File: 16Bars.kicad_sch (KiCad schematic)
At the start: 47 parts, among them IC1 CD4033BE, IC2 CD4033BE, IC3 CD4510BE, IC4 CD4510BE, IC5 CD4510BE, J1 3.5mm_Mono_Switched, J2 Conn_02x05_Odd_Even, Q1 2N3904, Q2 2N3904, Q3 2N3904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

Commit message: Fabrication Output for Rev 2.0
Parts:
- C1: footprint Capacitor_THT:C_Radial_D5.0mm_H11.0mm_P2.00mm -> Capacitor_THT:CP_Radial_D5.0mm_P2.00mm
- C11: Manufacturer_Part_Number (none) -> C13533
- C2, C3, C4, C5, C6: Manufacturer_Part_Number (none) -> C1525
- D1, D3, D4, D5: Manufacturer_Part_Number (none) -> C191023
- D2: Manufacturer_Part_Number (none) -> C2290
- Q1, Q2, Q3: Manufacturer_Part_Number (none) -> C9634
- R1, R11, R13, R14, R16, R17, R18, R19, R2, R20, R3, R4, R6: Manufacturer_Part_Number (none) -> C25744
- R10, R7, R8, R9: LCSC (none) -> C25744; Manufacturer_Part_Number (none) -> C25744
- R12, R15: Manufacturer_Part_Number (none) -> C4109
- R5: Manufacturer_Part_Number (none) -> C25792
- SW2: value SW_SPDT - EG1249 -> SW_SPDT-EG1249
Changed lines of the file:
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@@
+      (effects (font (size 1.27 1.27)) hide)
+    )
+    (property "Manufacturer_Part_Number" "C9634" (id 5) (at 228.6 133.35 0)
       (effects (font (size 1.27 1.27)) hide)
     )
@@
       (effects (font (size 1.27 1.27)) hide)
     )
+    (property "LCSC" "C25744" (id 4) (at 54.61 134.62 0)
+      (effects (font (size 1.27 1.27)) hide)
+    )
+    (property "Manufacturer_Part_Number" "C25744" (id 5) (at 54.61 134.62 0)
+      (effects (font (size 1.27 1.27)) hide)
+    )
     (pin "1")
     (pin "2")
@@
     )
     (property "LCSC" "C25744" (id 4) (at 127 128.27 90)
+      (effects (font (size 1.27 1.27)) hide)
+    )
+    (property "Manufacturer_Part_Number" "C25744" (id 5) (at 127 128.27 0)
       (effects (font (size 1.27 1.27)) hide)
     )
@@
       (effects (font (size 1.27 1.27)) hide)
     )
+    (property "Manufacturer_Part_Number" "C25744" (id 5) (at 194.31 29.21 0)
+      (effects (font (size 1.27 1.27)) hide)
+    )
     (pin "1")
     (pin "2")
@@
       (effects (font (size 1.27 1.27)) hide)
     )
+    (property "Manufacturer_Part_Number" "C25744" (id 5) (at 132.08 33.02 0)
+      (effects (font (size 1.27 1.27)) hide)
+    )
     (pin "1")
     (pin "2")
@@
       (effects (font (size 1.27 1.27)) hide)
     )
+    (property "Manufacturer_Part_Number" "C191023" (id 5) (at 45.72 26.67 0)
+      (effects (font (size 1.27 1.27)) hide)
+    )
     (pin "1")
     (pin "2")
@@
     )
     (property "LCSC" "C25744" (id 4) (at 135.89 119.38 90)
+      (effects (font (size 1.27 1.27)) hide)
+    )
+    (property "Manufacturer_Part_Number" "C25744" (id 5) (at 135.89 119.38 0)
       (effects (font (size 1.27 1.27)) hide)
     )
@@
       (effects (font (size 1.27 1.27)) (justify left))
     )
-    (property "Value" "SW_SPDT - EG1249" (id 1) (at 82.55 69.8499 0)
+    (property "Value" "SW_SPDT-EG1249" (id 1) (at 82.55 69.8499 0)
       (effects (font (size 1.27 1.27)) (justify left))
     )
@@
       (effects (font (size 1.27 1.27)) (justify left))
     )
-    (property "Footprint" "Capacitor_THT:C_Radial_D5.0mm_H11.0mm_P2.00mm" (id 2) (at 41.91 180.34 0)
+    (property "Footprint" "Capacitor_THT:CP_Radial_D5.0mm_P2.00mm" (id 2) (at 41.91 180.34 0)
       (effects (font (size 1.27 1.27)) hide)
     )
@@
     )
     (property "Datasheet" "~" (id 3) (at 24.13 134.62 0)
+      (effects (font (size 1.27 1.27)) hide)
+    )
+    (property "LCSC" "C25744" (id 4) (at 24.13 134.62 0)
+      (effects (font (size 1.27 1.27)) hide)
+    )
+    (property "Manufacturer_Part_Number" "C25744" (id 5) (at 24.13 134.62 0)
       (effects (font (size 1.27 1.27)) hide)
     )
@@
       (effects (font (size 1.27 1.27)) hide)
     )
+    (property "Manufacturer_Part_Number" "C191023" (id 5) (at 120.65 102.87 0)
+      (effects (font (size 1.27 1.27)) hide)
+    )
     (pin "1")
     (pin "2")
@@
     )
     (property "LCSC" "C9634" (id 4) (at 133.35 132.08 0)
+      (effects (font (size 1.27 1.27)) hide)
+    )
+    (property "Manufacturer_Part_Number" "C9634" (id 5) (at 133.35 132.08 0)
       (effects (font (size 1.27 1.27)) hide)
     )
@@
       (effects (font (size 1.27 1.27)) hide)
     )
+    (property "Manufacturer_Part_Number" "C1525" (id 5) (at 177.8 62.23 0)
+      (effects (font (size 1.27 1.27)) hide)
+    )
     (pin "1")
     (pin "2")
@@
       (effects (font (size 1.27 1.27)) hide)
     )
+    (property "Manufacturer_Part_Number" "C1525" (id 5) (at 181.61 24.13 0)
+      (effects (font (size 1.27 1.27)) hide)
+    )
     (pin "1")
     (pin "2")
@@
       (effects (font (size 1.27 1.27)) hide)
     )
+    (property "Manufacturer_Part_Number" "C25744" (id 5) (at 219.71 133.35 0)
+      (effects (font (size 1.27 1.27)) hide)
+    )
     (pin "1")
     (pin "2")
@@
     )
     (property "LCSC" "C25744" (id 4) (at 238.76 128.27 90)
+      (effects (font (size 1.27 1.27)) hide)
+    )
+    (property "Manufacturer_Part_Number" "C25744" (id 5) (at 238.76 128.27 0)
       (effects (font (size 1.27 1.27)) hide)
     )
@@
       (effects (font (size 1.27 1.27)) hide)
     )
+    (property "Manufacturer_Part_Number" "C25744" (id 5) (at 26.67 35.56 0)
+      (effects (font (size 1.27 1.27)) hide)
+    )
     (pin "1")
     (pin "2")
@@
     )
     (property "LCSC" "C1525" (id 4) (at 76.2 130.81 90)
+      (effects (font (size 1.27 1.27)) hide)
+    )
+    (property "Manufacturer_Part_Number" "C1525" (id 5) (at 76.2 130.81 0)
       (effects (font (size 1.27 1.27)) hide)
     )
@@
       (effects (font (size 1.27 1.27)) hide)
     )
+    (property "Manufacturer_Part_Number" "C25744" (id 5) (at 231.14 124.46 0)
+      (effects (font (size 1.27 1.27)) hide)
+    )
     (pin "1")
     (pin "2")
@@
     )
     (property "LCSC" "C25744" (id 4) (at 250.19 119.38 90)
+      (effects (font (size 1.27 1.27)) hide)
+    )
+    (property "Manufacturer_Part_Number" "C25744" (id 5) (at 250.19 119.38 0)
       (effects (font (size 1.27 1.27)) hide)
     )
@@
       (effects (font (size 1.27 1.27)) hide)
     )
+    (property "Manufacturer_Part_Number" "C25744" (id 5) (at 35.56 31.75 0)
+      (effects (font (size 1.27 1.27)) hide)
+    )
     (pin "1")
     (pin "2")
@@
       (effects (font (size 1.27 1.27)) hide)
     )
+    (property "LCSC" "C25744" (id 4) (at 26.67 134.62 0)
+      (effects (font (size 1.27 1.27)) hide)
+    )
+    (property "Manufacturer_Part_Number" "C25744" (id 5) (at 26.67 134.62 0)
+      (effects (font (size 1.27 1.27)) hide)
+    )
     (pin "1")
     (pin "2")
@@
     )
     (property "LCSC" "C4109" (id 4) (at 93.98 134.62 90)
+      (effects (font (size 1.27 1.27)) hide)
+    )
+    (property "Manufacturer_Part_Number" "C4109" (id 5) (at 93.98 134.62 0)
       (effects (font (size 1.27 1.27)) hide)
     )
@@
     )
     (property "LCSC" "C25744" (id 4) (at 85.09 53.34 90)
+      (effects (font (size 1.27 1.27)) hide)
+    )
+    (property "Manufacturer_Part_Number" "C25744" (id 5) (at 85.09 53.34 0)
       (effects (font (size 1.27 1.27)) hide)
     )
@@
       (effects (font (size 1.27 1.27)) hide)
     )
+    (property "Manufacturer_Part_Number" "C25792" (id 5) (at 198.12 133.35 0)
+      (effects (font (size 1.27 1.27)) hide)
+    )
     (pin "1")
     (pin "2")
@@
     )
     (property "Datasheet" "~" (id 3) (at 57.15 134.62 0)
+      (effects (font (size 1.27 1.27)) hide)
+    )
+    (property "LCSC" "C25744" (id 4) (at 57.15 134.62 0)
+      (effects (font (size 1.27 1.27)) hide)
+    )
+    (property "Manufacturer_Part_Number" "C25744" (id 5) (at 57.15 134.62 0)
       (effects (font (size 1.27 1.27)) hide)
     )
@@
     )
     (property "LCSC" "C9634" (id 4) (at 247.65 128.27 0)
+      (effects (font (size 1.27 1.27)) hide)
+    )
+    (property "Manufacturer_Part_Number" "C9634" (id 5) (at 247.65 128.27 0)
       (effects (font (size 1.27 1.27)) hide)
     )
@@
       (effects (font (size 1.27 1.27)) hide)
     )
+    (property "Manufacturer_Part_Number" "C2290" (id 5) (at 38.1 199.39 0)
+      (effects (font (size 1.27 1.27)) hide)
+    )
     (pin "1")
     (pin "2")
@@
     )
     (property "LCSC" "C191023" (id 4) (at 205.74 133.35 0)
+      (effects (font (size 1.27 1.27)) hide)
+    )
+    (property "Manufacturer_Part_Number" "C191023" (id 5) (at 205.74 133.35 0)
       (effects (font (size 1.27 1.27)) hide)
     )
@@
       (effects (font (size 1.27 1.27)) hide)
     )
+    (property "Manufacturer_Part_Number" "C25744" (id 5) (at 193.04 73.66 0)
+      (effects (font (size 1.27 1.27)) hide)
+    )
     (pin "1")
     (pin "2")
@@
     )
     (property "LCSC" "C4109" (id 4) (at 49.53 199.39 90)
+      (effects (font (size 1.27 1.27)) hide)
+    )
+    (property "Manufacturer_Part_Number" "C4109" (id 5) (at 49.53 199.39 0)
       (effects (font (size 1.27 1.27)) hide)
     )
@@
     )
     (property "LCSC" "C1525" (id 4) (at 45.72 135.89 90)
+      (effects (font (size 1.27 1.27)) hide)
+    )
+    (property "Manufacturer_Part_Number" "C1525" (id 5) (at 45.72 135.89 0)
       (effects (font (size 1.27 1.27)) hide)
     )
@@
       (effects (font (size 1.27 1.27)) hide)
     )
+    (property "Manufacturer_Part_Number" "C191023" (id 5) (at 38.1 26.67 0)
+      (effects (font (size 1.27 1.27)) hide)
+    )
     (pin "1")
     (pin "2")
@@
       (effects (font (size 1.27 1.27)) hide)
     )
+    (property "Manufacturer_Part_Number" "C1525" (id 5) (at 34.29 54.61 0)
+      (effects (font (size 1.27 1.27)) hide)
+    )
     (pin "1")
     (pin "2")
@@
       (effects (font (size 1.27 1.27)) hide)
     )
+    (property "Manufacturer_Part_Number" "C25744" (id 5) (at 129.54 73.66 0)
+      (effects (font (size 1.27 1.27)) hide)
+    )
     (pin "1")
     (pin "2")
@@
     )
     (property "LCSC" "C13533" (id 4) (at 215.9 135.89 0)
+      (effects (font (size 1.27 1.27)) hide)
+    )
+    (property "Manufacturer_Part_Number" "C13533" (id 5) (at 215.9 135.89 0)
       (effects (font (size 1.27 1.27)) hide)
     )
@@
     )
     (path "/5f506440-0fcc-449f-9242-db683d2fb800"
-      (reference "C1") (unit 1) (value "47uf") (footprint "Capacitor_THT:C_Radial_D5.0mm_H11.0mm_P2.00mm")
+      (reference "C1") (unit 1) (value "47uf") (footprint "Capacitor_THT:CP_Radial_D5.0mm_P2.00mm")
     )
     (path "/e2092cd4-73b6-42b3-9f2c-6392bcbbe00b"
@@
     )
     (path "/54155070-a256-4c8f-a67e-f02182028ef1"
-      (reference "SW2") (unit 1) (value "SW_SPDT - EG1249") (footprint "EG1249")
+      (reference "SW2") (unit 1) (value "SW_SPDT-EG1249") (footprint "EG1249")
     )
     (path "/41613b88-4d66-4377-a8c7-96e52cc4c696"

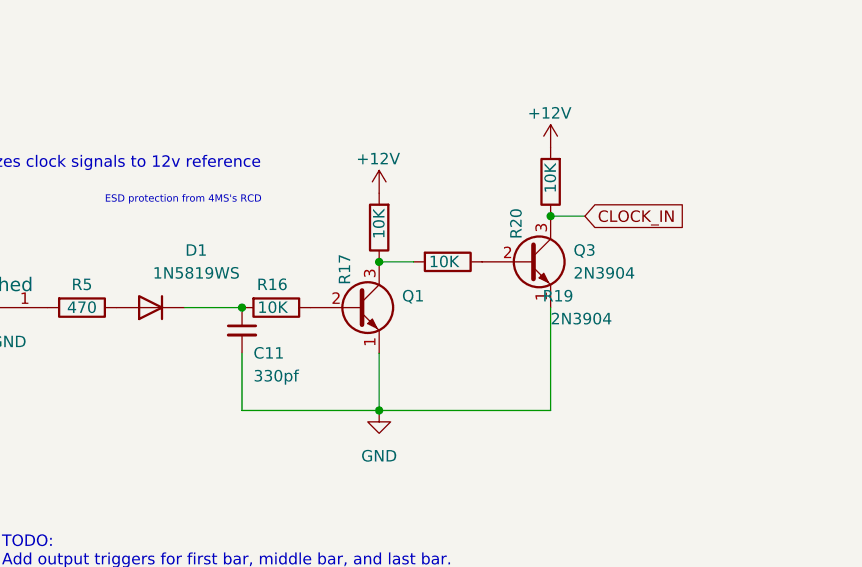
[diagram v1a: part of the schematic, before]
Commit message: DC offset might be the issue
CLOCK_IN is in an always on state, need to scope the incoming signal to find out for sure.
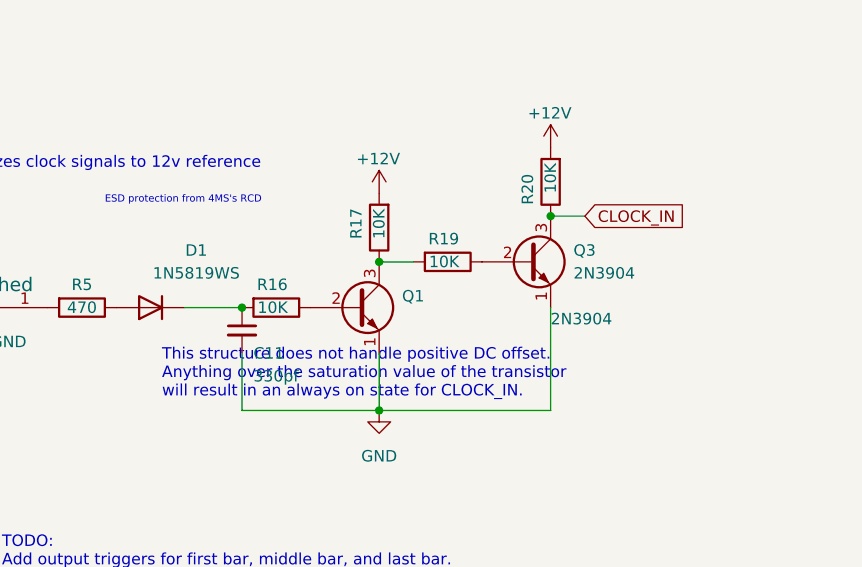
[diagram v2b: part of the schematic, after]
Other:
- note added: "This structure does not handle positive DC offset. Anything over the saturation value of the transistor will result in an always on state for CLOCK_IN."
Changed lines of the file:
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@@
     (effects (font (size 2 2)) (justify left bottom))
+  )
+  (text "This structure does not handle positive DC offset.\nAnything over the saturation value of the transistor\nwill result in an always on state for CLOCK_IN."
+    (at 207.01 143.51 0)
+    (effects (font (size 1.27 1.27)) (justify left bottom))
   )
   (label "BarCountCarry" (at 26.67 82.55 0)
@@
   (symbol (lib_id "Device:R") (at 238.76 128.27 270) (unit 1)
     (in_bom yes) (on_board yes)
-    (property "Reference" "R19" (id 0) (at 252.73 132.08 90)
+    (property "Reference" "R19" (id 0) (at 240.03 125.73 90)
       (effects (font (size 1.27 1.27)) (justify right))
     )
@@
   (symbol (lib_id "Device:R") (at 231.14 124.46 180) (unit 1)
     (in_bom yes) (on_board yes)
-    (property "Reference" "R17" (id 0) (at 227.33 130.81 90)
+    (property "Reference" "R17" (id 0) (at 228.6 125.73 90)
       (effects (font (size 1.27 1.27)) (justify right))
     )
@@
   (symbol (lib_id "Device:R") (at 250.19 119.38 180) (unit 1)
     (in_bom yes) (on_board yes)
-    (property "Reference" "R20" (id 0) (at 246.38 125.73 90)
-      (effects (font (size 1.27 1.27)) (justify right))
-    )
+    (property "Reference" "R20" (id 0) (at 247.65 121.92 90)
+      (effects (font (size 1.27 1.27)) (justify right))
+    )

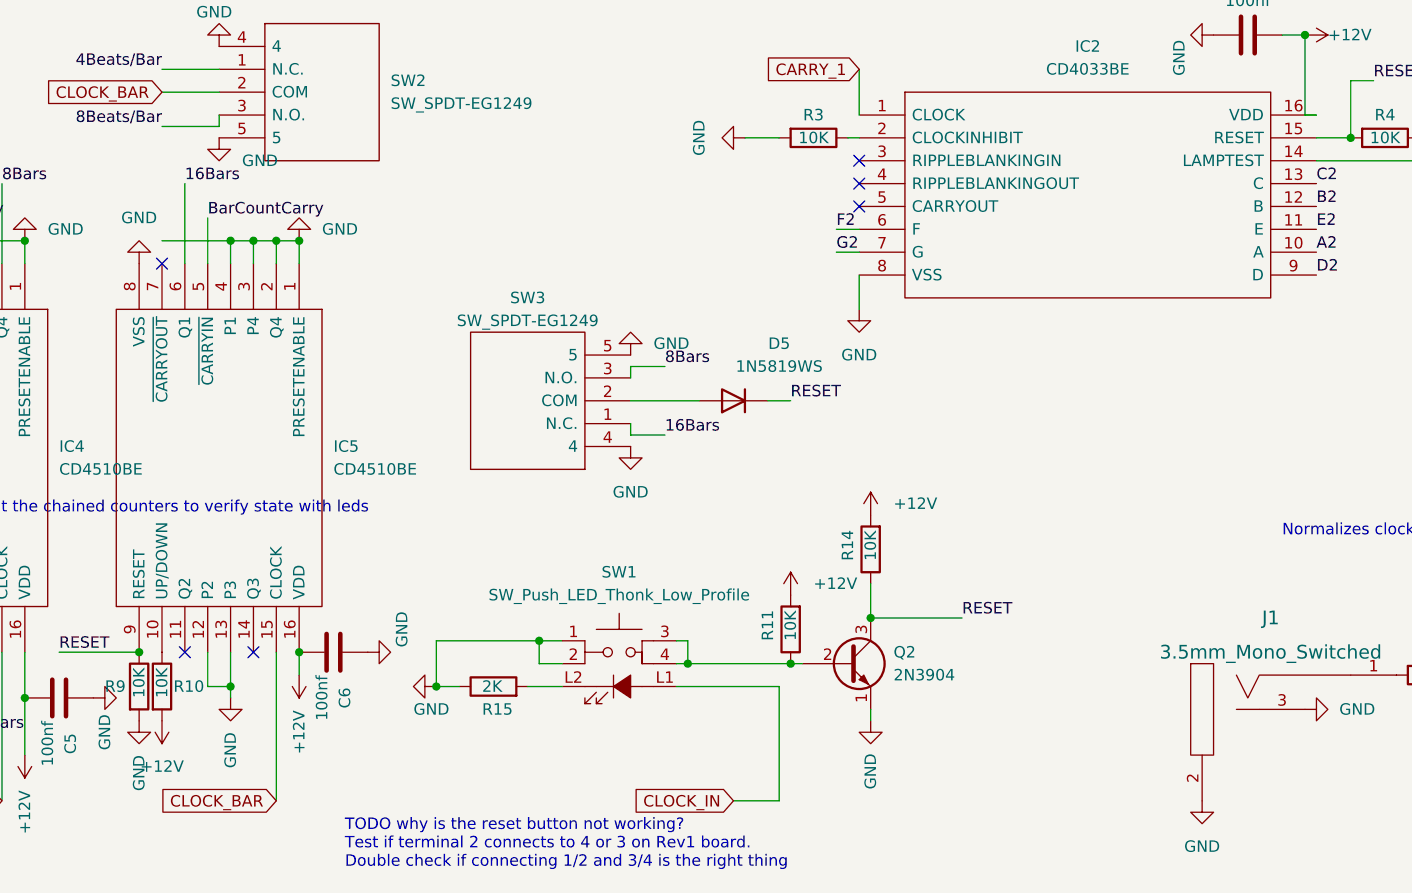
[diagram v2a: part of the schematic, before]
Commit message: Add 16Bar reset AND logic transistor to schematic
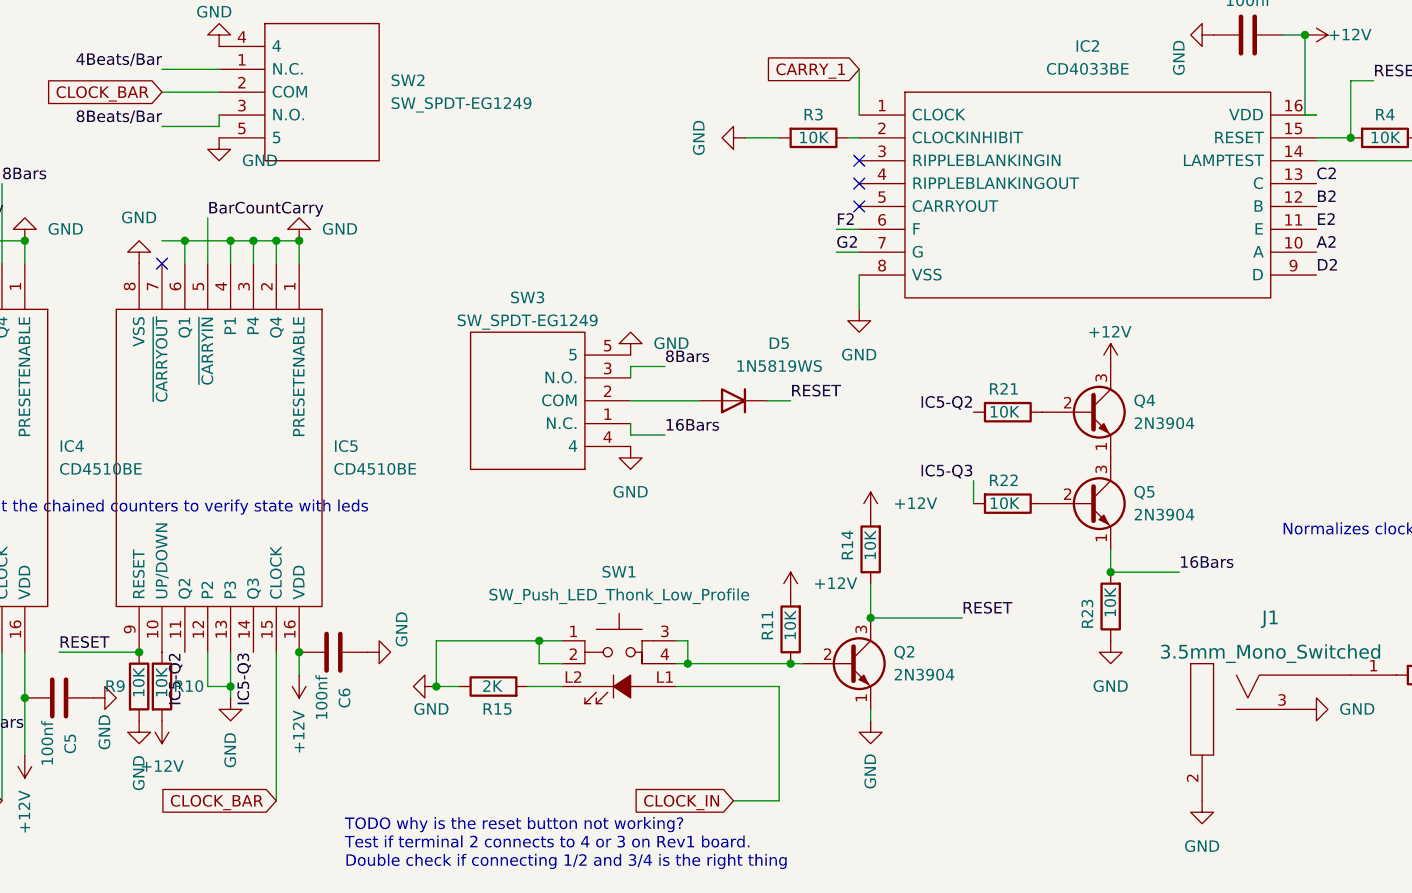
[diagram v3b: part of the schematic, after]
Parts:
- added Q4, Q5: 2N3904, Package_TO_SOT_SMD:SOT-89-3, symbol Transistor_BJT:2N3904
- added R21, R22, R23: 10K, Resistor_SMD:R_0402_1005Metric, symbol Device:R
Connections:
- net +12V: now also Q4.3 (C)
- net 16Bars: now also Q5.1 (E), R23.2; no longer IC5.6 (Q1)
- net GND: now also IC5.6 (Q1), R23.1
- net IC5-Q2: now reaches IC5.11 (Q2)
- net IC5-Q2: now also R21.2
- net IC5-Q3: now reaches IC5.14 (Q3)
- net IC5-Q3: now also R22.2
- new net: Q4.2 (B), R21.1
- new net: Q5.2 (B), R22.1
- new net: Q4.1 (E), Q5.3 (C)
- no-connect marks 14 -> 12
